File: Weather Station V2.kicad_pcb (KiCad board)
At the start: 4 copper layers, 106.5 x 67.2 mm, 57 parts, among them J1 SOLAR IN, J2 18650, J3 Battery_AUX, J5 SENSORS, J6 USB_C, J7 RYLR998, J8 Breakout, Q1 AO4842, Q2 DMP2240UDM-7, SW1 LED_ENABLE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

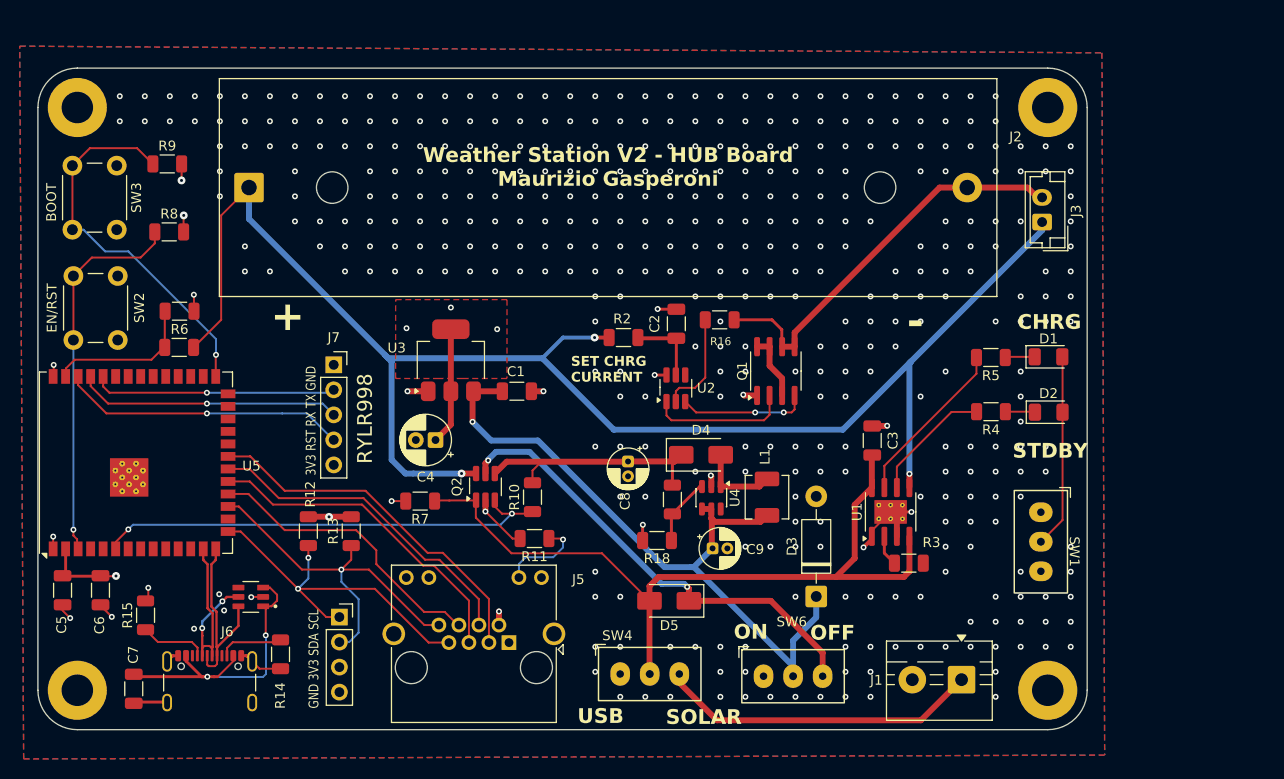
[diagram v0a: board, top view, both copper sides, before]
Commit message: Replaced RJ45 with 1x8 P1.25mm JST connector Fix: line ends normalization for kicad files
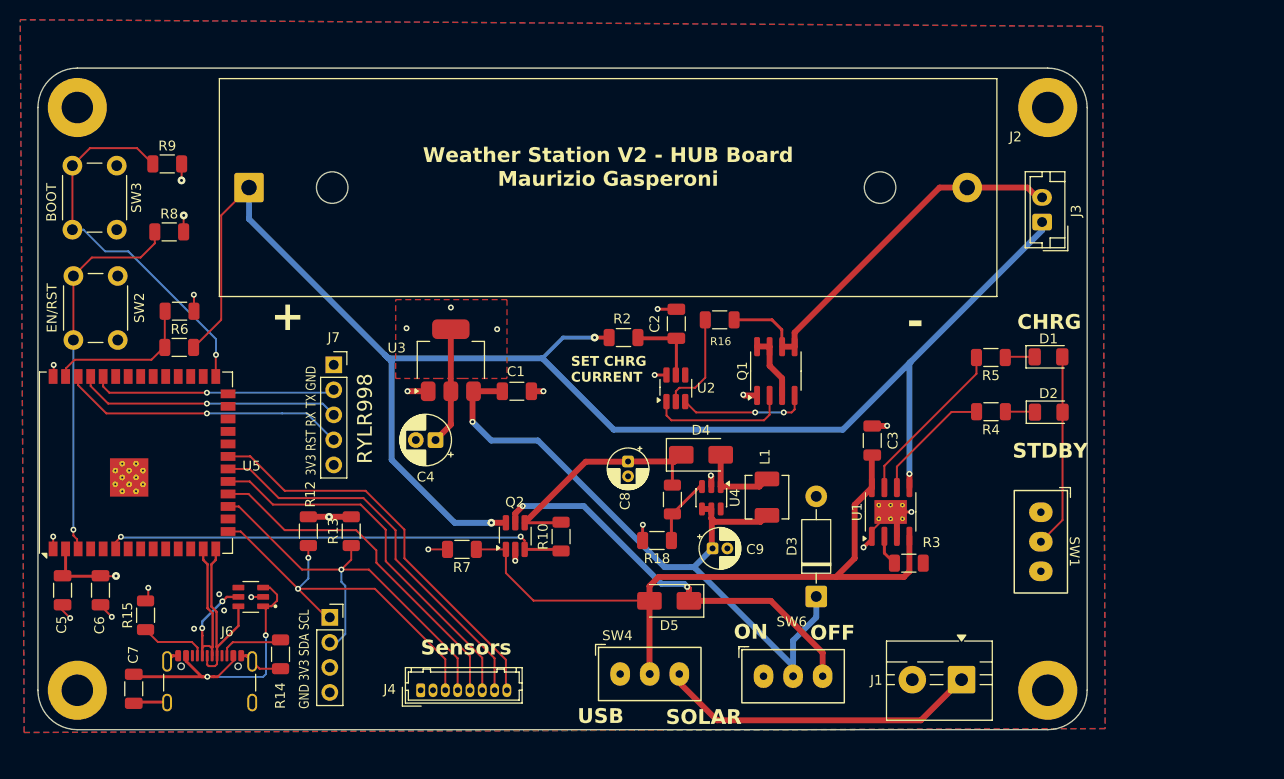
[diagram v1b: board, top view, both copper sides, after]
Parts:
- removed J5: SENSORS, Connector_RJ:RJ45_Amphenol_RJHSE538X
- removed R11: 150, Resistor_SMD:R_1206_3216Metric
- added J4: Conn_01x08_Socket, Connector_Hirose:Hirose_DF13-08P-1.25DSA_1x08_P1.25mm_Vertical, F.Cu at (127.3, 121.0)
- moved R7 6.48 mm to (131.5, 106.7)
- moved Q2 5.84 mm to (136.9, 105.3)
- moved R10 4.94 mm to (141.6, 105.3)
- moved J8 0.98 mm to (118.1, 113.5)
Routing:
- net Net-(J5-Pad10): track 8.83 -> 0.00 mm, vias 1 -> 0
- net /GPIO12: track 33.6 -> 40.0 mm
- net /Vin: track 80.6 -> 74.7 mm
- net /W_SPEED: track 29.8 -> 35.6 mm
- net Net-(D5-K): track 47.4 -> 41.8 mm
- net /BAT+: track 161.6 -> 166.7 mm
- net /GPIO13: track 36.9 -> 41.6 mm
- net /GPIO11: track 33.7 -> 38.4 mm
- net /SDA: track 39.8 -> 44.4 mm
- net /SCL: track 37.3 -> 39.8 mm
- net Net-(J4-Pin_1): track 20.5 -> 18.3 mm
- net GND: track 44.2 -> 42.8 mm, vias 409 -> 20
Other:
- board text added: "Sensors"

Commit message: Added breakoout board - no panelization done yet Manufacturing capabilities have not been checked
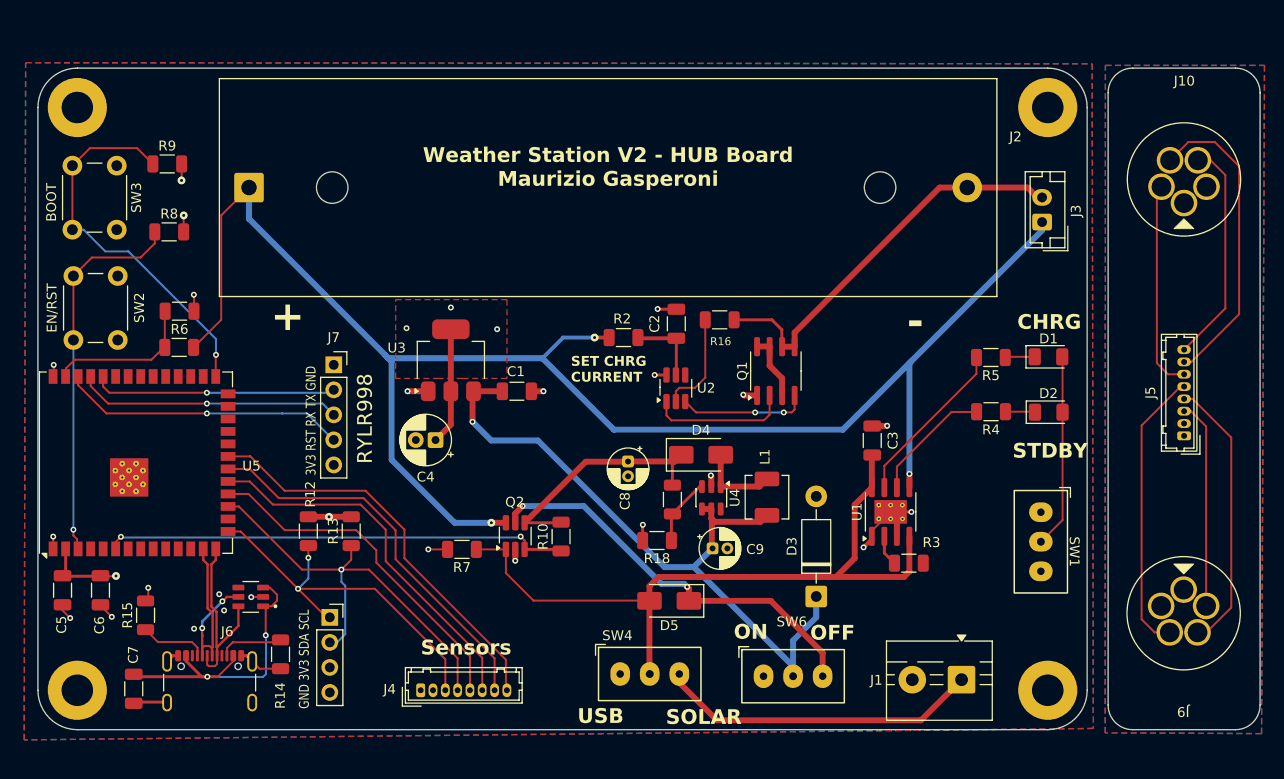
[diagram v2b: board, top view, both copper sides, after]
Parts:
- added J10: SP13 Socket, SP13_5pin_holes:SP13_5pin_holes, F.Cu at (204.8, 69.1)
- added J5: Conn_01x08_Socket, Connector_Hirose:Hirose_DF13-08P-1.25DSA_1x08_P1.25mm_Vertical, F.Cu at (204.8, 95.1)
- added J9: SP13 Socket, SP13_5pin_holes:SP13_5pin_holes, F.Cu at (204.8, 113.1)
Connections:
- net Net-(J4-Pin_1) renamed /Sensors Interface/5V Sensors
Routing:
- net /Sensors Interface/5V - Breakout: track 0.00 -> 41.1 mm
- net /Sensors Interface/GPIO12 - Breakout: track 0.00 -> 31.4 mm
- net /Sensors Interface/WSPEED - Breakout: track 0.00 -> 29.0 mm
- net /Sensors Interface/SDA - Breakout: track 0.00 -> 28.1 mm
- net /Sensors Interface/GPIO13 - Breakout: track 0.00 -> 22.9 mm
- net /Sensors Interface/GPIO11 - Breakout: track 0.00 -> 21.3 mm
- net /Sensors Interface/SCL - Breakout: track 0.00 -> 21.1 mm
- added copper zone on B.Cu, net GND1
- added copper zone on F.Cu, net GND1
- added copper zone on In1.Cu, net GND1
- added copper zone on In2.Cu, net GND1
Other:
- board size 106.5 x 67.2 mm -> 124 x 67.2 mm

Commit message: Added esp32 connection to charging status lines (CHRG 48, STDBY 47) Panelization with breakout board. Potentially final. Proably sending it soon
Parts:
- added M1: ~, PCM_JLCPCB:MouseBites, Cosmetic, JLCPCB, 1.6mm, F.Cu at (195.0, 94.7)
- added M2: ~, PCM_JLCPCB:MouseBites, Cosmetic, JLCPCB, 1.6mm, F.Cu at (195.0, 119.4)
- added M3: ~, PCM_JLCPCB:MouseBites, Cosmetic, JLCPCB, 1.6mm, F.Cu at (195.0, 69.8)
- added M4: ~, PCM_JLCPCB:MouseBites, Cosmetic, JLCPCB, 1.6mm, F.Cu at (195.0, 82.0)
- added M5: ~, PCM_JLCPCB:MouseBites, Cosmetic, JLCPCB, 1.6mm, F.Cu at (195.0, 107.2)
- moved J10 0.55 mm to (204.3, 69.3)
- moved J9 0.55 mm to (204.3, 113.3)
- moved J5 0.55 mm to (204.3, 95.3)
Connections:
- U5 pad 25: unconnected-(U5-IO48-Pad25) -> /STDBY
- U5 pad 26: unconnected-(U5-IO45-Pad26) -> /CHRG
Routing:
- net /STDBY: track 12.5 -> 98.3 mm, vias 0 -> 4
- net /CHRG: track 17.1 -> 100.6 mm, vias 0 -> 2
- removed copper zone on B.Cu, net GND1
- removed copper zone on F.Cu, net GND1
- removed copper zone on In2.Cu, net GND1
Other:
- board size 124 x 67.2 mm -> 123.5 x 67.3 mm

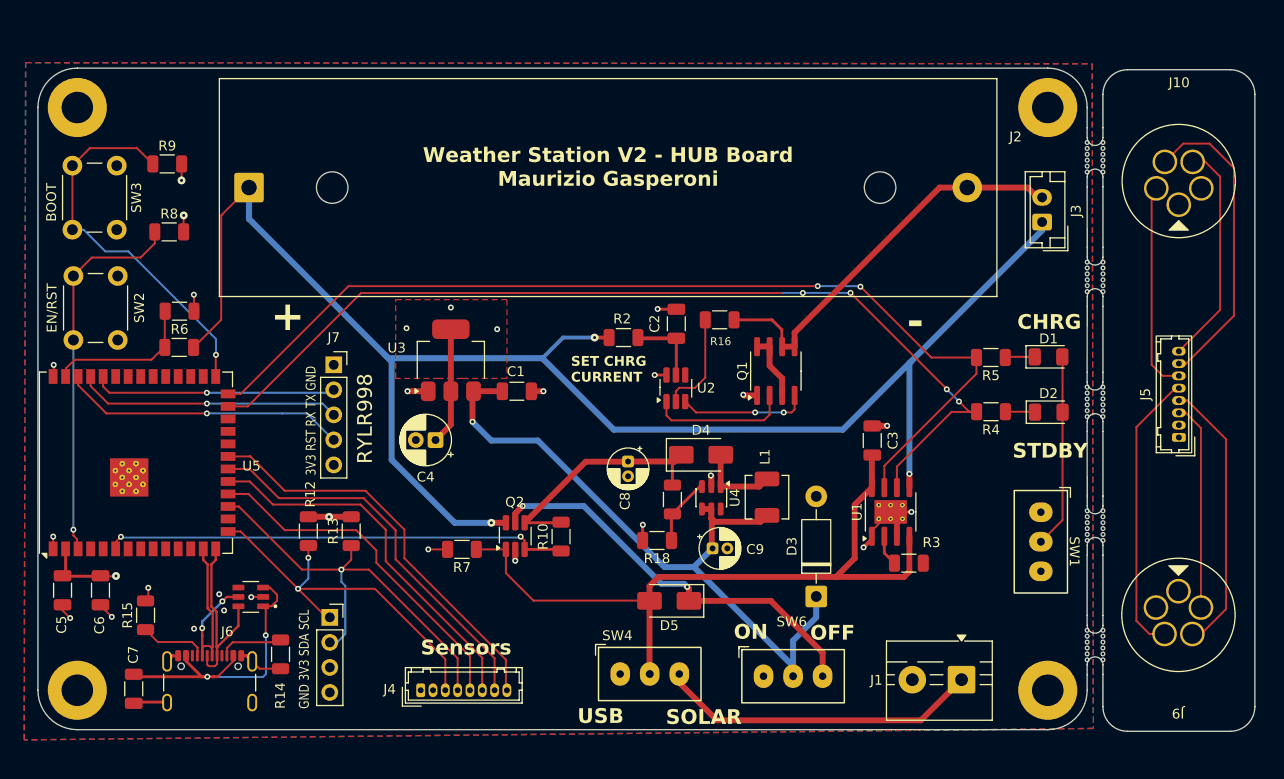
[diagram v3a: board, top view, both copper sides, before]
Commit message: Now sensor power gets switched before 5V boost-coverter Reduced 3.3v plane size
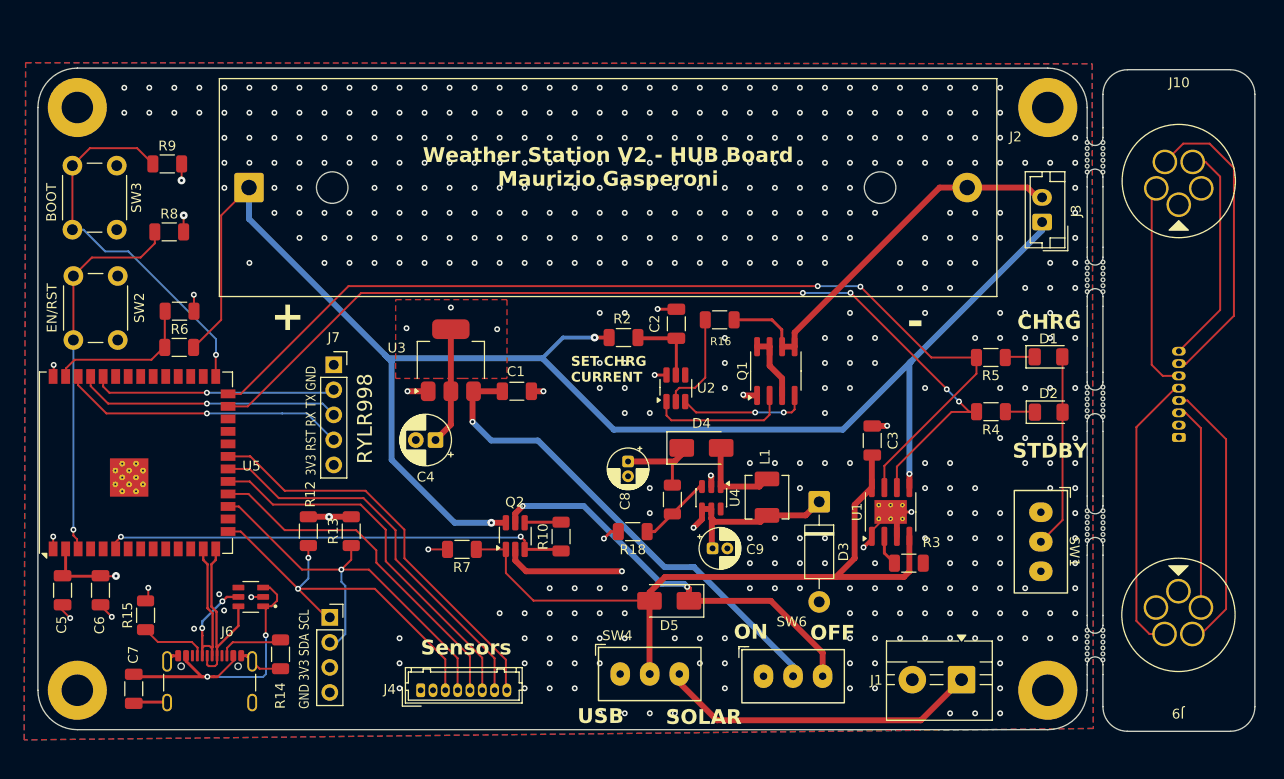
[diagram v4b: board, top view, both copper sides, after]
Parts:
- J5: moved to B.Cu
- moved D3 9.61 mm to (167.8, 101.8), turned to -90 degrees
- moved R18 2.62 mm to (148.9, 104.8)
- moved D4 0.70 mm to (155.8, 96.3)
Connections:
- C1 pad 1: /PWR_ToSensors -> /BatteryReg
- C9 pad 1: /PWR_ToSensors -> Net-(D3-K)
- D3 pad 1: /PWR_ToSensors -> Net-(D3-K)
- J4 pad 1: /Sensors Interface/5V Sensors -> +5V
- L1 pad 1: /PWR_ToSensors -> Net-(D3-K)
- Q2 pad 2: /Sensors Interface/5V Sensors -> Net-(D3-K)
- Q2 pad 4: +5V -> /PWR_ToSensors
- R10 pad 2: +5V -> /PWR_ToSensors
- SW6 pad 2: /PWR_ToSensors -> /BatteryReg
- U3 pad 3: /PWR_ToSensors -> /BatteryReg
- U4 pad 4: /PWR_ToSensors -> Net-(D3-K)
- U4 pad 5: /PWR_ToSensors -> Net-(D3-K)
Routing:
- net /PWR_ToSensors: track 72.9 -> 3.81 mm, vias 1 -> 0
- net /BatteryReg: track 0.00 -> 50.2 mm, vias 0 -> 1
- net Net-(D3-K): track 0.00 -> 40.6 mm, vias 0 -> 2
- net /Sensors Interface/5V Sensors: track 18.3 -> 0.00 mm, vias 1 -> 0
- net +5V: track 26.9 -> 41.2 mm
- net +3V3: track 80.7 -> 79.7 mm
- net Net-(D4-A): track 8.25 -> 8.97 mm
- net Net-(U4-FB): track 6.89 -> 7.46 mm
- net GND: track 42.8 -> 42.9 mm, vias 20 -> 432

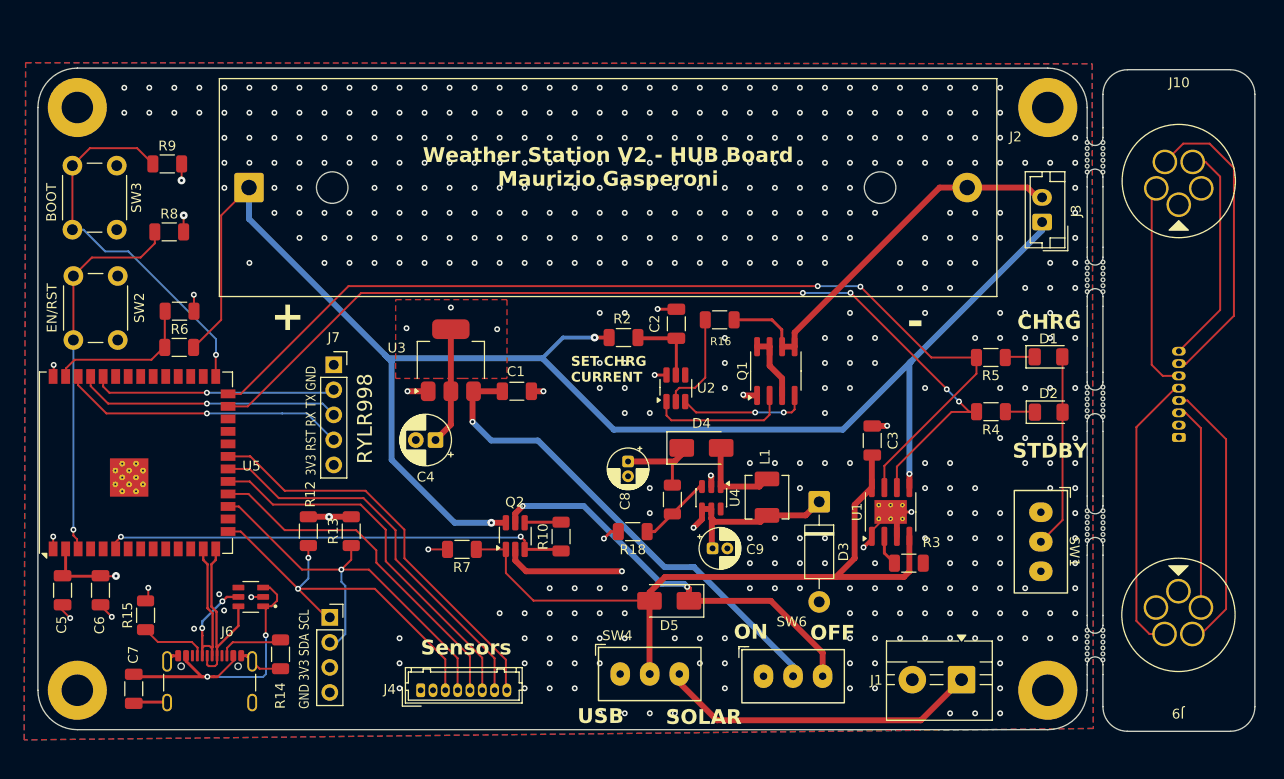
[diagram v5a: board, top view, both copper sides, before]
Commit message: - Changed CHRG and STDBY pins to 48 and 47 (CHRG was strapping) - Exposed 5V rail do Breakout connector. Now also it matches a bme280 pinout for testing - Renamed BatteryReg net to Battery_SW - Fixed connection to 5V converter - Changed to USBLC6-2SC6 for ESD Protection - Fixed mirrored VEML7700 footprint
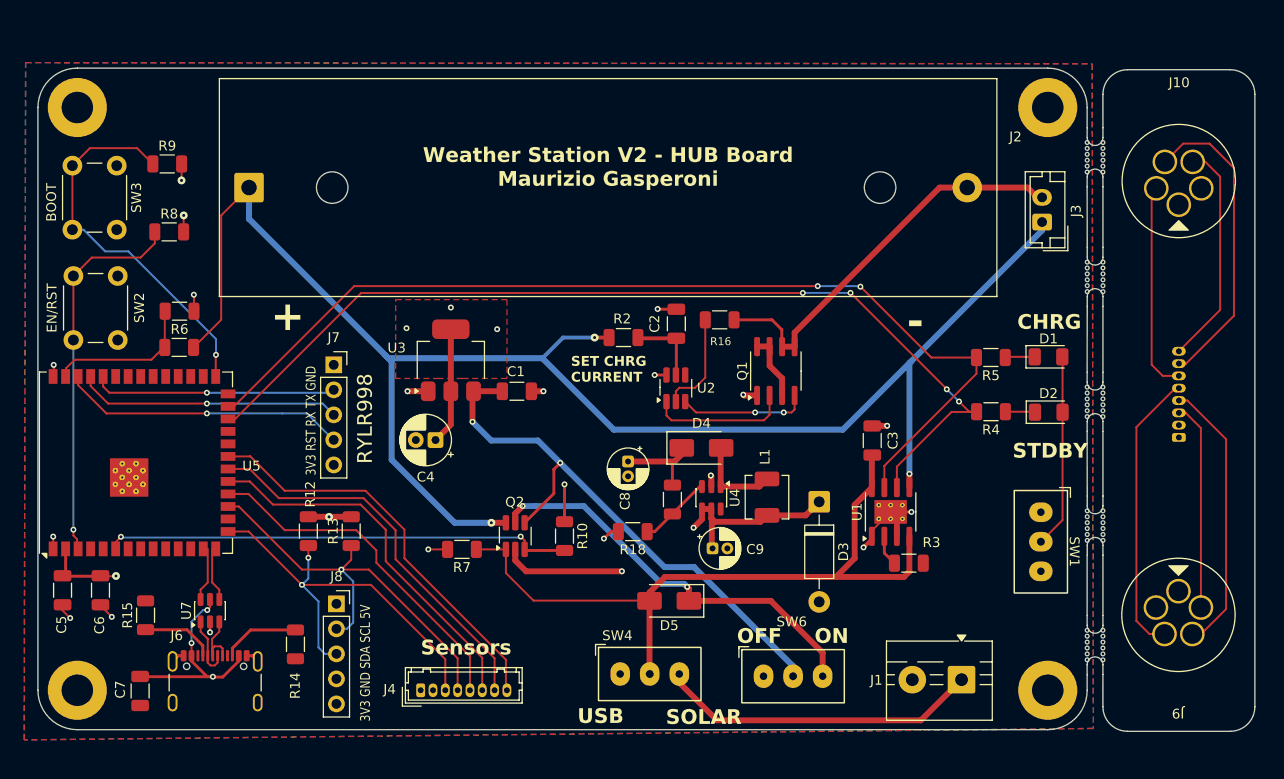
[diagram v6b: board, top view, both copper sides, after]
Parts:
- removed U6: TPD3S014DBVR, TPD3S014DBVR:SOT95P280X145-6N
- added U7: USBLC6-2SC6, Package_TO_SOT_SMD:SOT-23-6, F.Cu at (105.9, 112.9)
- J8: footprint Connector_PinSocket_2.54mm:PinSocket_1x04_P2.54mm_Vertical -> Connector_PinSocket_2.54mm:PinSocket_1x05_P2.54mm_Vertical
- moved R14 1.82 mm to (114.6, 116.3)
- moved J8 1.53 mm to (118.8, 112.2)
- moved C7 0.68 mm to (98.9, 121.0), turned to -90 degrees
- moved J6 0.56 mm to (106.5, 121.1)
- moved R10 0.35 mm to (141.9, 105.3), turned to -90 degrees
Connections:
- C1 pad 1: /BatteryReg -> /Battery_SW
- C7 pad 1: GND -> Net-(SW4-A)
- C7 pad 2: Net-(SW4-A) -> GND
- J6 pad A6: /D+ -> /IN_D+
- J6 pad A7: /D- -> /IN_D-
- J6 pad B6: /D+ -> /IN_D+
- J6 pad B7: /D- -> /IN_D-
- J8 pad 1: /SCL -> +5V
- J8 pad 3: +3V3 -> /SCL
- Q2 pad 3: /SENSOR_EN -> /~{SENSOR_EN}
- Q2 pad 4: /PWR_ToSensors -> /Battery_SW
- R10 pad 1: /SENSOR_EN -> +3V3
- R10 pad 2: /PWR_ToSensors -> /~{SENSOR_EN}
- SW6 pad 2: /BatteryReg -> /Battery_SW
- U3 pad 3: /BatteryReg -> /Battery_SW
- U5 pad 24: unconnected-(U5-IO47-Pad24) -> /STDBY
- U5 pad 25: /STDBY -> /CHRG
- U5 pad 26: /CHRG -> unconnected-(U5-IO45-Pad26)
- U5 pad 6: /SENSOR_EN -> /~{SENSOR_EN}
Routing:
- net /Battery_SW: track 0.00 -> 57.8 mm, vias 0 -> 2
- net /BatteryReg: track 50.2 -> 0.00 mm, vias 1 -> 0
- net /~{SENSOR_EN}: track 0.00 -> 47.7 mm, vias 0 -> 2
- net /SENSOR_EN: track 47.4 -> 0.00 mm, vias 2 -> 0
- net /D-: track 23.9 -> 5.45 mm, vias 2 -> 0
- net +5V: track 41.2 -> 55.6 mm
- net /D+: track 19.7 -> 5.45 mm
- net Net-(SW4-A): track 78.7 -> 66.8 mm, vias 2 -> 3
- net GND: track 42.9 -> 34.8 mm, vias 432 -> 17
- net /IN_D+: track 0.00 -> 6.53 mm
- net /IN_D-: track 0.00 -> 6.51 mm
- net /SCL: track 39.8 -> 44.0 mm
- net /PWR_ToSensors: track 3.81 -> 0.00 mm
- net +3V3: track 79.7 -> 83.5 mm, vias 7 -> 8
- net Net-(J6-CC2): track 6.16 -> 7.93 mm
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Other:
- board text added: "3V3 GND SDA SCL 5V"
- board text removed: "GND 3V3 SDA SCL"
